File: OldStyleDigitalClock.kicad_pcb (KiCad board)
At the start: 2 copper layers, 175 x 105 mm, 89 parts, among them J1 USB_A_OUT, J2 USB_A_OUT, J3 USB_C_IN, SW1 Set minutes, SW2 Set hours, U1 4071, U10 CD4026BE, U11 NE555D, U12 CD4060BE, U13 CD4017BE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

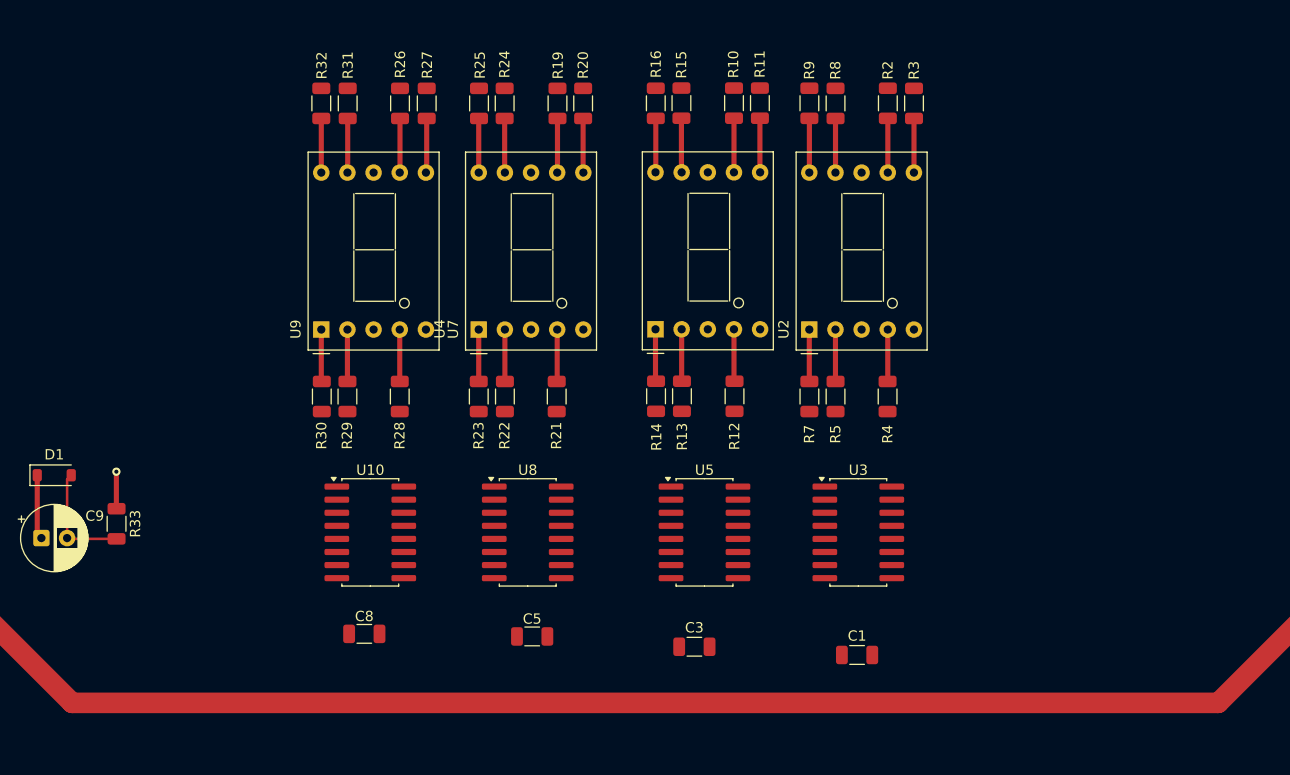
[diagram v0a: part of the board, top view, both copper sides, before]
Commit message: segment tracks started
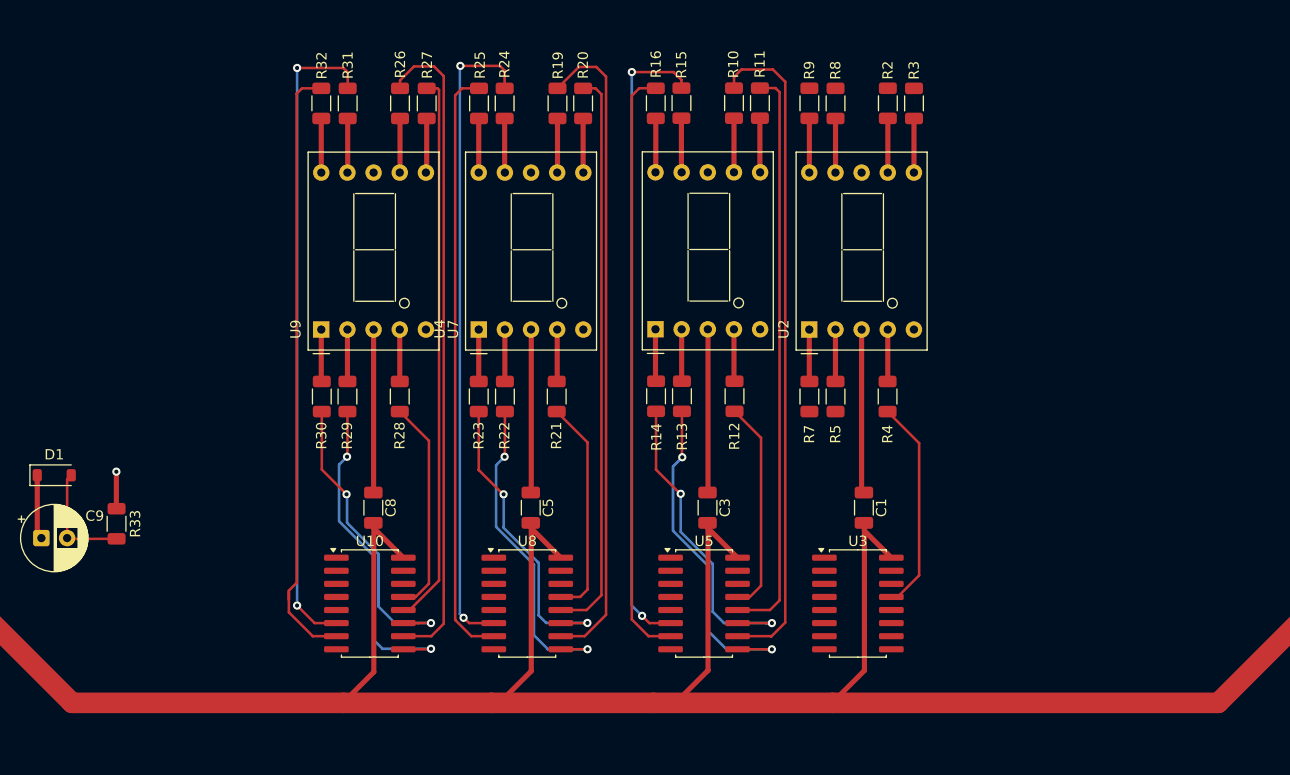
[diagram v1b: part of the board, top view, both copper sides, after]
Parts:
- moved C1 14.3 mm to (136.7, 78.4), turned to 90 degrees
- moved C3 13.6 mm to (121.6, 78.4), turned to 90 degrees
- moved C5 12.5 mm to (104.4, 78.4), turned to 90 degrees
- moved C8 12.3 mm to (89.1, 78.4), turned to 90 degrees
- moved U10 6.91 mm to (88.8, 87.7)
- moved U3 6.91 mm to (136.2, 87.7)
- moved U5 6.91 mm to (121.2, 87.7)
- moved U8 6.91 mm to (104.0, 87.7)
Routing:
- net +5V: track 335.0 -> 431.1 mm
- net Net-(U5-A): track 0.00 -> 64.6 mm
- net Net-(U10-A): track 0.00 -> 63.6 mm
- net Net-(U8-A): track 0.00 -> 63.5 mm
- net GND: track 139.7 -> 203.1 mm
- net Net-(U10-F): track 0.00 -> 63.4 mm, vias 0 -> 2
- net Net-(U8-F): track 0.00 -> 63.1 mm, vias 0 -> 2
- net Net-(U5-F): track 0.00 -> 62.2 mm, vias 0 -> 2
- net Net-(U10-G): track 0.00 -> 59.6 mm
- net Net-(U8-G): track 0.00 -> 57.9 mm
- net Net-(U5-G): track 0.00 -> 57.9 mm
- net Net-(U5-B): track 0.00 -> 55.9 mm
- net Net-(U8-B): track 0.00 -> 55.2 mm
- net Net-(U10-B): track 0.00 -> 53.6 mm
- net Net-(U5-D): track 0.00 -> 33.4 mm, vias 0 -> 2
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
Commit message: More tracks
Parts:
- moved C9 11.0 mm to (61.2, 91.4)
- moved D1 11.0 mm to (62.5, 85.3)
- moved R33 11.0 mm to (68.5, 90.0)
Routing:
- net Net-(U3-A): track 0.00 -> 64.6 mm
- net Net-(U3-F): track 0.00 -> 62.2 mm, vias 0 -> 2
- net Net-(U3-G): track 0.00 -> 58.1 mm
- net Net-(U3-B): track 0.00 -> 55.7 mm
- net Net-(U3-D): track 0.00 -> 31.6 mm, vias 0 -> 2
- net Net-(U3-E): track 0.00 -> 30.8 mm, vias 0 -> 2
- net Net-(U8-E): track 29.9 -> 30.8 mm
- net Net-(U5-D): track 33.4 -> 32.5 mm
- net Net-(U10-E): track 29.7 -> 30.5 mm
- net Net-(U10-D): track 32.5 -> 31.7 mm
- net Net-(U8-F): track 63.1 -> 63.9 mm

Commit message: Fixed issue in MR circuit. More tracks.
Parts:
- moved C6 215.4 mm to (158.2, 83.5), turned to -90 degrees
- moved U1 200.9 mm to (151.8, 88.9), turned to 0 degrees
- moved C7 98.2 mm to (69.2, 75.2), turned to -90 degrees
- moved U6 83.4 mm to (62.5, 80.5), turned to 0 degrees
- moved C17 80.3 mm to (53.1, 32.5)
- moved C18 80.3 mm to (53.1, 42.9)
- moved U13 80.3 mm to (61.1, 34.0)
- moved U14 80.3 mm to (61.1, 44.7)
- moved U15 80.3 mm to (61.1, 55.5)
- moved C19 78.6 mm to (53.0, 50.8), turned to 90 degrees
- moved C4 74.0 mm to (174.7, 47.4)
- moved R18 74.0 mm to (174.7, 52.2)
- moved SW2 74.0 mm to (162.9, 47.7)
- moved SW1 73.6 mm to (162.9, 63.2)
- moved R17 72.6 mm to (164.3, 43.6), turned to 180 degrees
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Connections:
- D1 pad 1: +5V -> MR
- D1 pad 2: MR -> GND
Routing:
- net 1_MIN_CLK: track 0.00 -> 198.5 mm
- net MR: track 11.1 -> 161.6 mm, vias 0 -> 3
- net +5V: track 431.1 -> 511.6 mm
- net GND: track 203.1 -> 277.2 mm, vias 10 -> 15
- net Net-(C4-Pad2): track 15.1 -> 63.1 mm, vias 0 -> 1
- net Net-(U3-CARRY_OUT): track 0.00 -> 36.7 mm, vias 0 -> 2
- net Net-(U10-DISPLAY_EN_IN): track 0.00 -> 36.2 mm, vias 0 -> 2
- net Net-(U3-DISPLAY_EN_OUT): track 0.00 -> 36.1 mm, vias 0 -> 2
- net /CLK 1/(10 hours): track 0.00 -> 35.9 mm, vias 0 -> 2
- net Net-(U5-DISPLAY_EN_OUT): track 0.00 -> 35.3 mm, vias 0 -> 2
- net Net-(C2-Pad2): track 16.3 -> 40.3 mm, vias 0 -> 1
- net /Time/CLK 2 Hz: track 12.8 -> 23.1 mm
- net Net-(U5-RESET): track 0.00 -> 2.50 mm, vias 0 -> 1
- net Net-(U3-C): track 20.7 -> 22.6 mm
- net Net-(U5-C): track 20.7 -> 22.6 mm
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
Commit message: Tracks partial
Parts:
- moved D4 55.6 mm to (121.2, 28.1)
- moved R37 52.6 mm to (111.2, 28.1)
- moved C11 49.9 mm to (153.5, 30.6)
- moved C12 49.9 mm to (147.8, 32.7)
- moved C13 49.9 mm to (161.9, 35.0)
- moved D3 49.9 mm to (160.7, 38.9)
- moved R34 49.9 mm to (149.4, 39.2)
- moved R38 49.9 mm to (161.3, 30.6)
- moved U11 49.9 mm to (155.0, 34.6)
- moved RV1 48.0 mm to (181.6, 29.4)
- moved H2 20.0 mm to (195.0, 105.0)
- moved H3 20.0 mm to (30.0, 105.0)
- moved C7 12.3 mm to (75.1, 64.4)
- moved U6 12.3 mm to (68.4, 69.7)
- moved C10 10.2 mm to (47.6, 66.1)
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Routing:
- net /CLK 1/(24 hours): track 0.00 -> 117.3 mm
- net Net-(U10-RESET): track 0.00 -> 90.1 mm, vias 0 -> 2
- net LED_PWM: track 6.69 -> 92.3 mm, vias 0 -> 2
- net Net-(U8-CLK): track 0.15 -> 63.4 mm
- net Net-(U5-E): track 31.5 -> 92.5 mm, vias 2 -> 3
- net Net-(U5-RESET): track 2.50 -> 42.5 mm, vias 1 -> 2
- net MR: track 161.6 -> 198.0 mm
- net Net-(D4-A): track 14.4 -> 49.9 mm
- net Net-(U3-CLK): track 0.00 -> 35.3 mm, vias 0 -> 2
- net +5V: track 511.6 -> 541.0 mm, vias 1 -> 2
- net 1_MIN_CLK: track 198.5 -> 171.2 mm
- net Net-(D3-A): track 30.9 -> 57.4 mm
- net Net-(D3-K): track 0.00 -> 23.2 mm
- net GND: track 277.2 -> 289.2 mm, vias 15 -> 17
- net /CLK 1/hour: track 0.00 -> 11.9 mm
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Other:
- board size 175 x 105 mm -> 175 x 85 mm

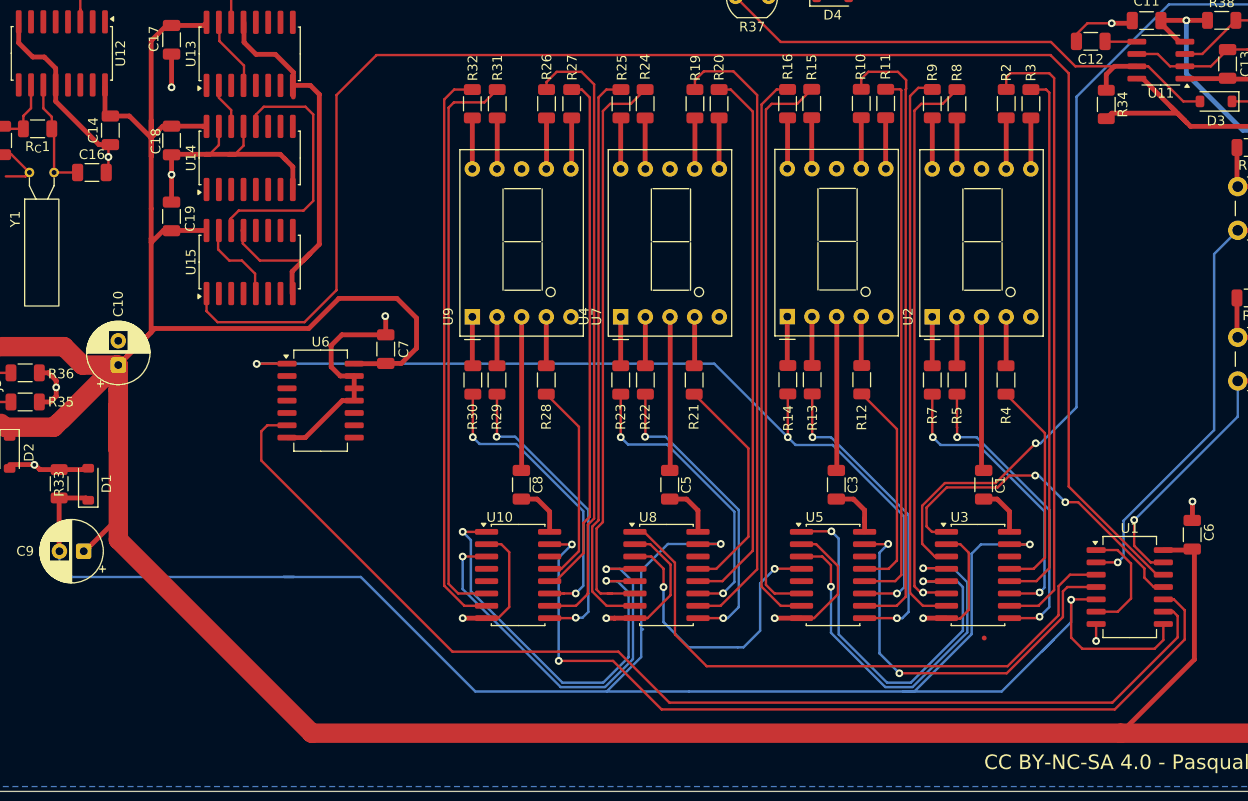
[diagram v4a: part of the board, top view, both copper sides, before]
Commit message: Tracks, first draft completed prior to design review
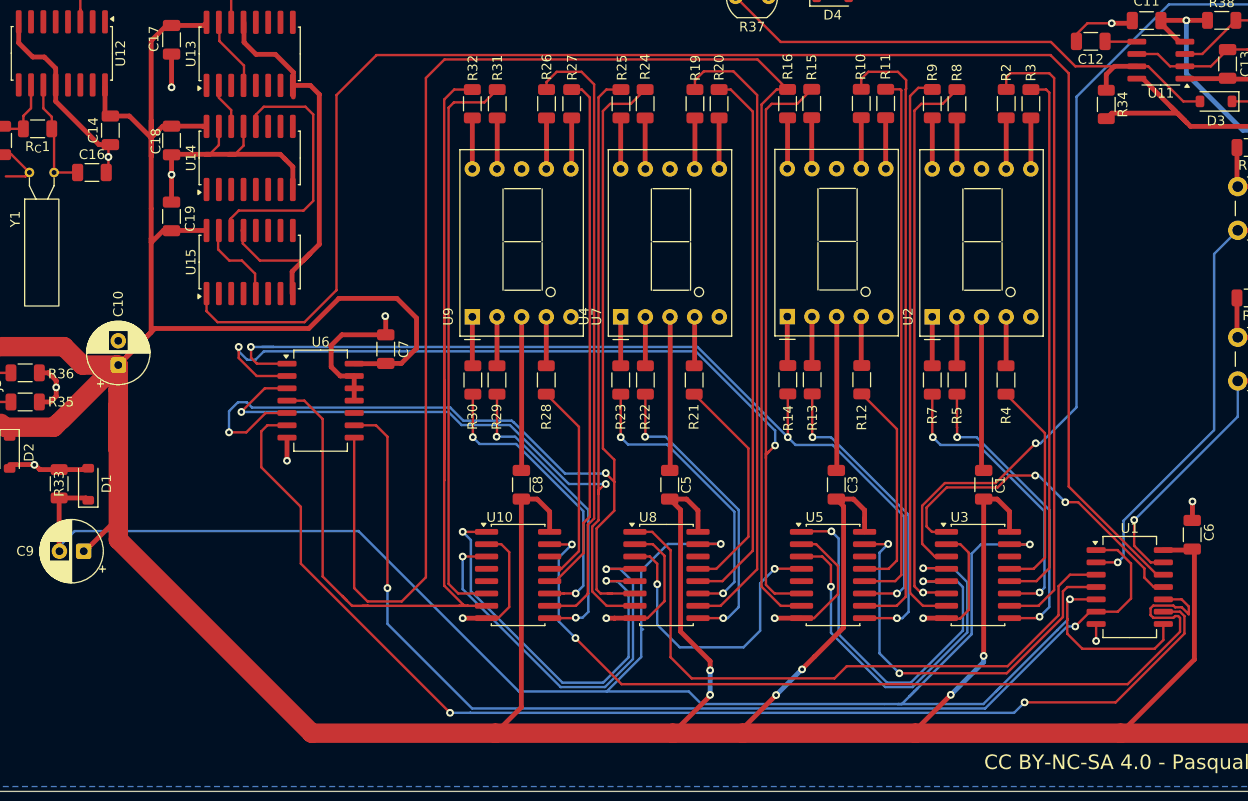
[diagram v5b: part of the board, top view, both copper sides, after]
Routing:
- net Net-(U5-G): track 57.9 -> 173.2 mm
- net +5V: track 541.0 -> 649.5 mm, vias 2 -> 8
- net /CLK 1/hour: track 11.9 -> 115.9 mm, vias 0 -> 2
- net Net-(U10-G): track 58.6 -> 129.7 mm
- net Net-(U5-F): track 58.6 -> 128.9 mm, vias 0 -> 2
- net Net-(U8-F): track 59.4 -> 112.8 mm, vias 0 -> 2
- net Net-(U8-G): track 58.8 -> 106.4 mm, vias 0 -> 2
- net GND: track 289.2 -> 282.7 mm, vias 17 -> 18
- net /CLK 1/(24 hours): track 117.3 -> 123.2 mm, vias 0 -> 2
- net Net-(U5-E): track 92.5 -> 97.4 mm
- net Net-(U10-RESET): track 90.1 -> 93.3 mm
- net Net-(U8-CLK): track 63.4 -> 66.6 mm
- net MR: track 198.0 -> 200.7 mm

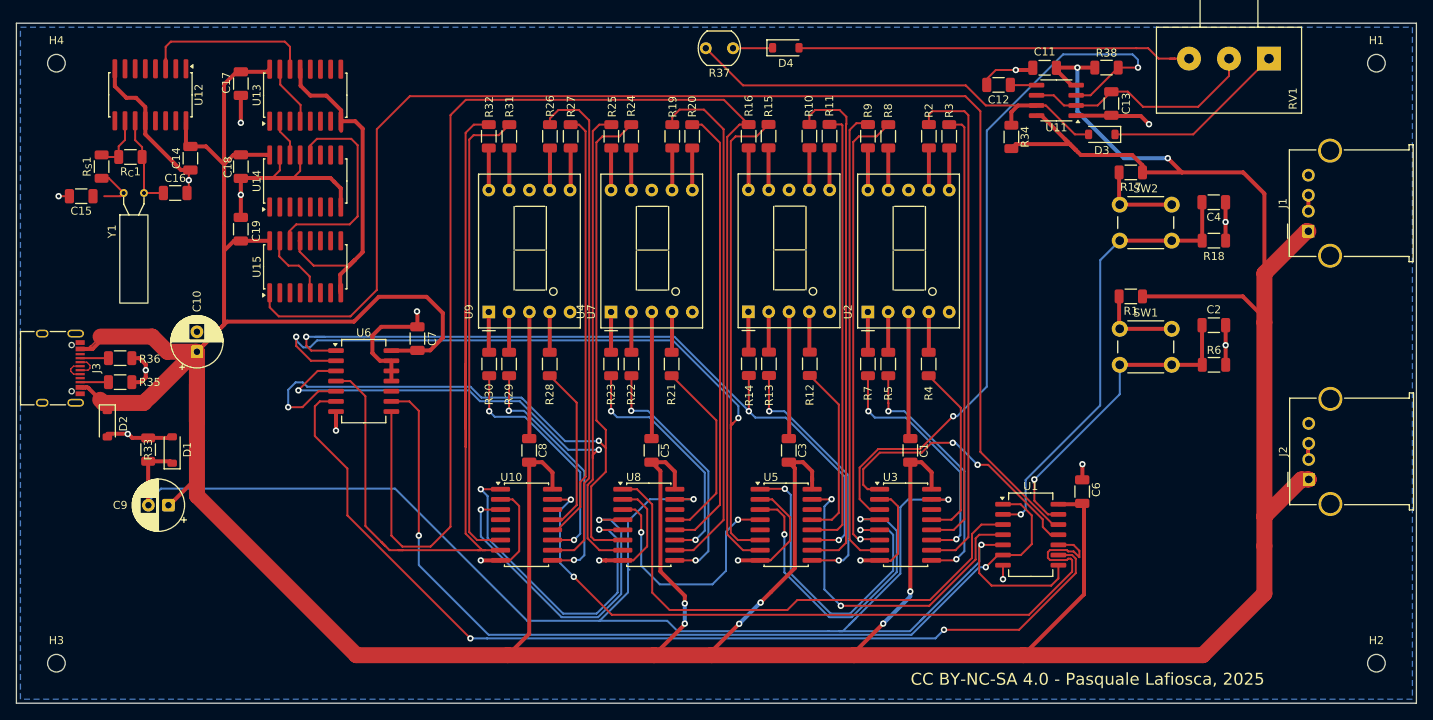
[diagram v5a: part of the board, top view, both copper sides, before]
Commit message: connected mounting holes to GND
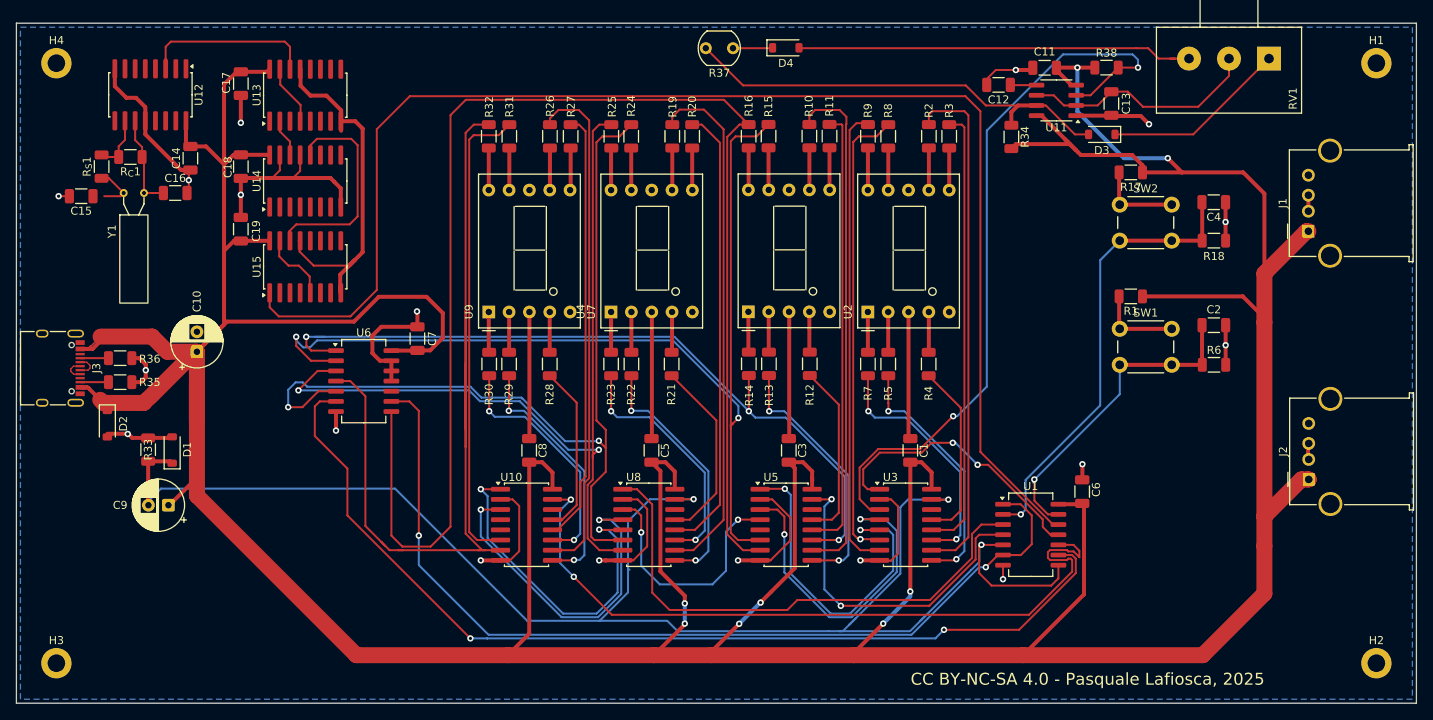
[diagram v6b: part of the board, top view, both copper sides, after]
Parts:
- H1, H2, H3, H4: footprint MountingHole:MountingHole_2.2mm_M2_DIN965 -> MountingHole:MountingHole_2.2mm_M2_DIN965_Pad
